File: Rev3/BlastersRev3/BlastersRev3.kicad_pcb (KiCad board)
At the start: 2 copper layers, 64 parts, among them SW1 Switch, SW10 Switch, SW11 Switch, SW12 Switch, SW13 Switch, SW14 Switch, SW15 Switch, SW16 Switch, SW17 Switch, SW18 Switch, SW19 Switch, SW2 Switch, SW20 Switch, SW21 Switch, SW22 Switch, SW23 Switch, SW24 Switch, SW25 Switch, SW26 Switch, SW27 Switch, SW28 Switch, SW29 Switch, SW3 Switch, SW30 Switch, SW4 Switch, SW5 Switch, SW6 Switch, SW7 Switch, SW8 Switch, SW9 Switch, U1 ProMicro

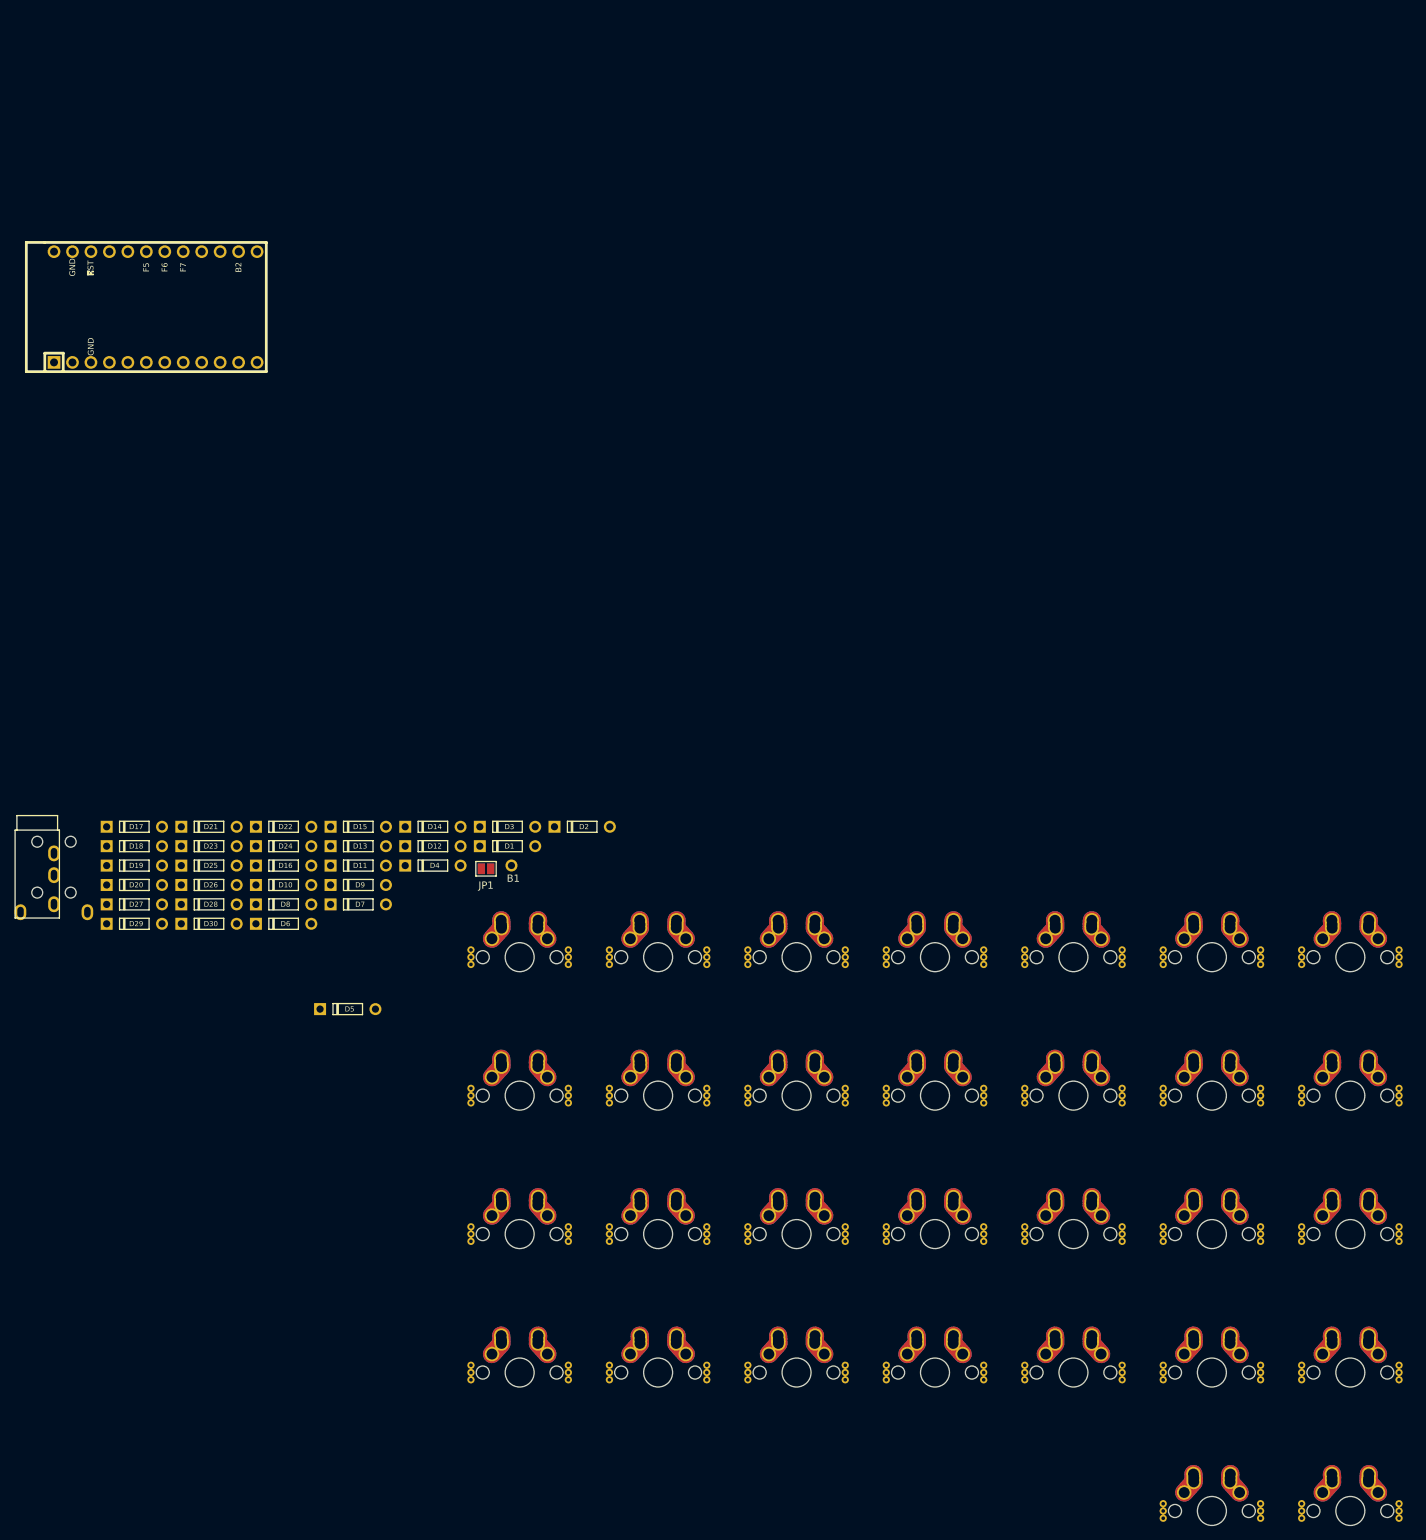
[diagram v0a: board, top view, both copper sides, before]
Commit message: Preliminary col routing done
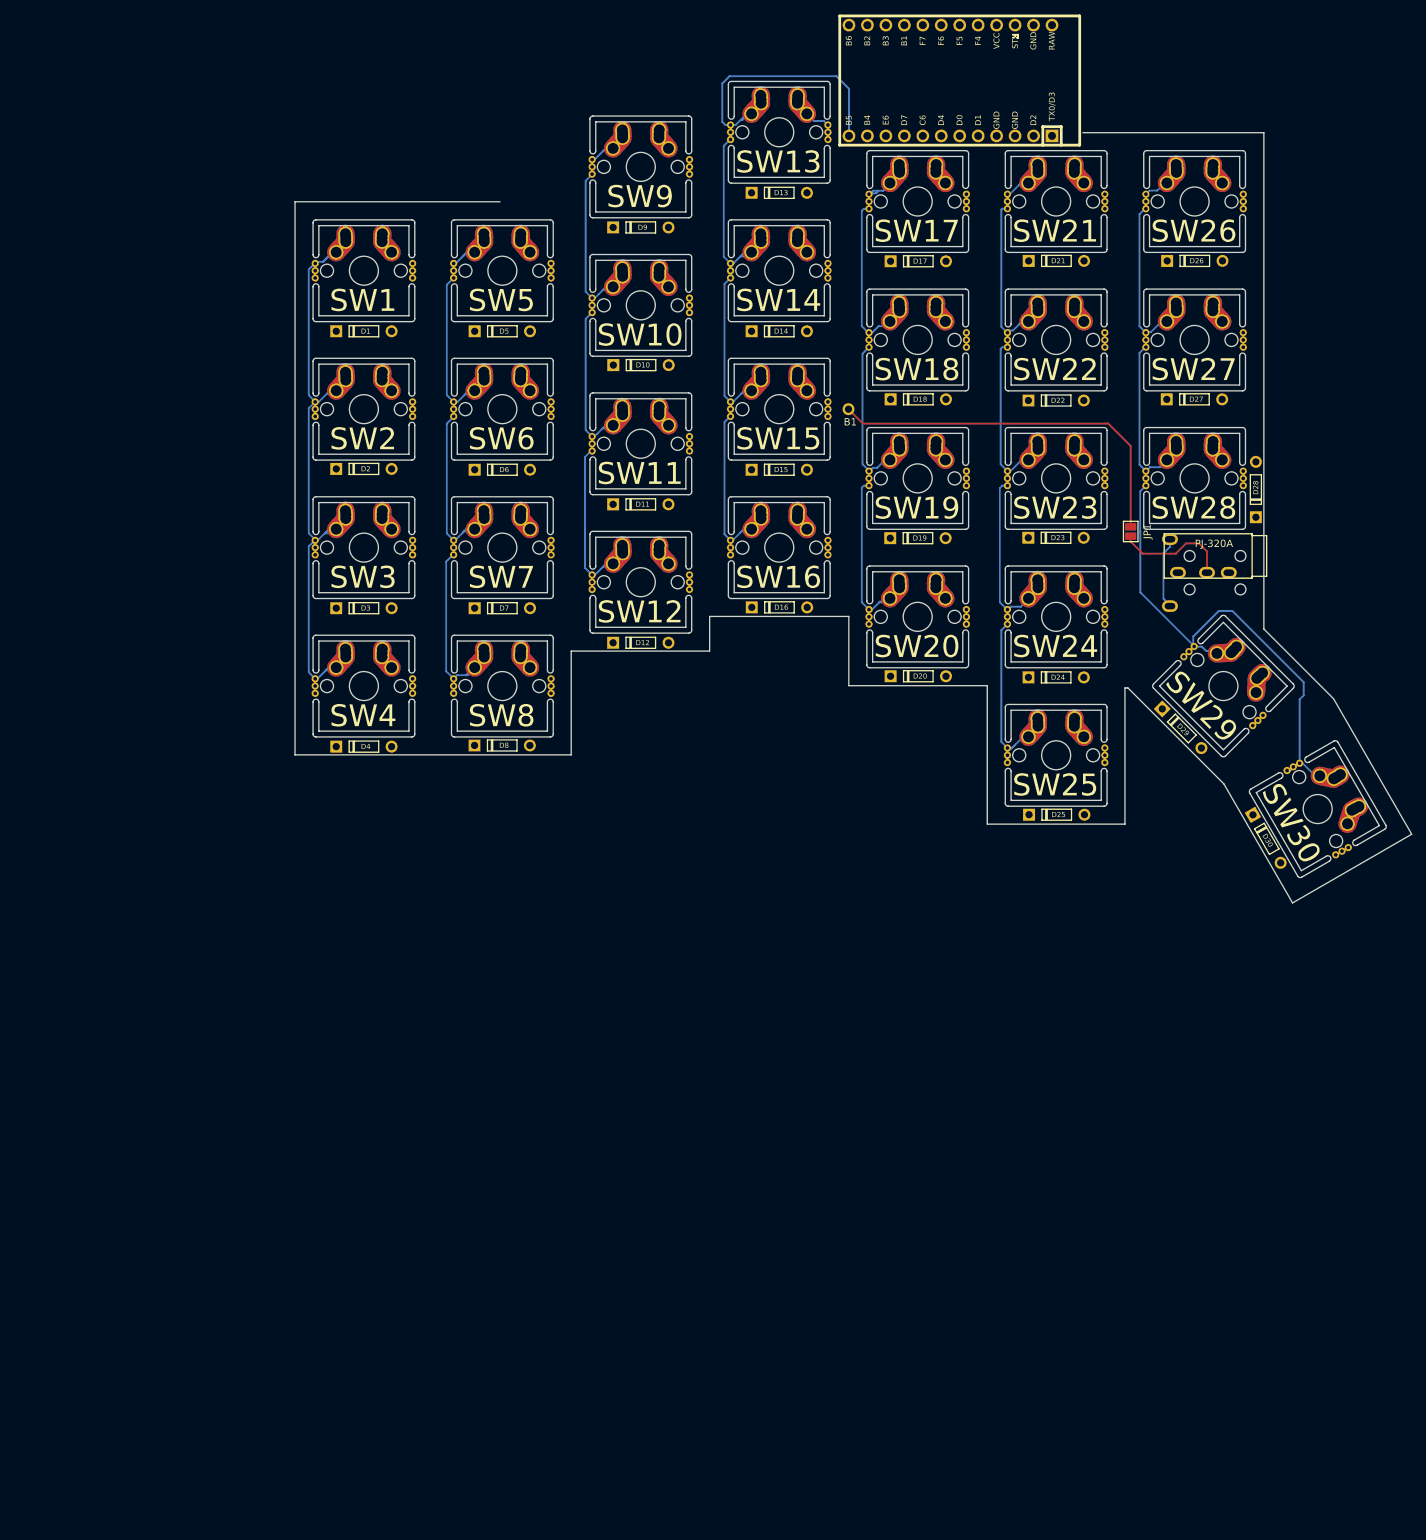
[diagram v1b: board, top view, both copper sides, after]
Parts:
- U1: moved to B.Cu
- moved PJ1 168.6 mm to (212.7, 96.3), turned to 270 degrees
- moved D27 161.6 mm to (204.8, 72.5)
- moved D26 160.5 mm to (204.8, 53.4)
- moved D28 154.9 mm to (213.2, 84.9), turned to 90 degrees
- moved D29 146.6 mm to (203.0, 117.8), turned to 315 degrees
- moved D30 146.0 mm to (214.7, 132.9), turned to 300 degrees
- moved D21 140.2 mm to (185.8, 53.4)
- moved D17 133.0 mm to (166.8, 53.5)
- moved D18 124.2 mm to (166.8, 72.5)
- moved D23 124.0 mm to (185.7, 91.5)
- moved D22 121.4 mm to (185.7, 72.6)
- moved D25 116.9 mm to (185.8, 129.6)
- moved D19 116.9 mm to (166.7, 91.6)
- moved SW14 115.5 mm to (147.6, 54.8)
- moved SW13 115.5 mm to (147.6, 35.7)
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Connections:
- U1 pad 12: (no net) -> Col3
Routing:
- net Col6: track 0.00 -> 143.0 mm
- net Col3: track 0.00 -> 135.7 mm
- net Col5: track 0.00 -> 133.3 mm
- net Col4: track 0.00 -> 116.3 mm
- net Col1: track 0.00 -> 109.5 mm
- net Col0: track 0.00 -> 105.3 mm
- net Col2: track 0.00 -> 102.9 mm
- net RGBBreakout: track 0.00 -> 52.0 mm
- net Net-(JP1-Pad1): track 0.00 -> 16.0 mm
- net CommVcc: track 0.00 -> 9.83 mm
- net Net-(D13-Pad1): track 0.00 -> 5.62 mm
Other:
- board outline added: 153.6 x 113 mm
